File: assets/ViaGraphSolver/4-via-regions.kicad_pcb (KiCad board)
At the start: 2 copper layers, 0 parts

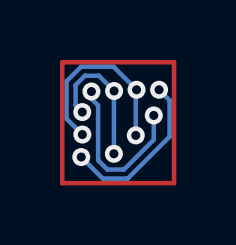
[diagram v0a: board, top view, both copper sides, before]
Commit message: Optimized 4  Via regions  Topology for  Improved Solve Performance
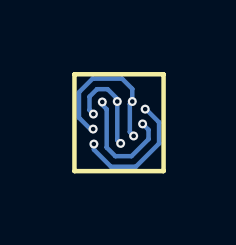
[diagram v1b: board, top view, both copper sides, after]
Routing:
- net net1: track 5.59 -> 3.92 mm
- net net4: track 4.71 -> 3.33 mm
- net net3: track 5.53 -> 4.27 mm
- net net5: track 6.40 -> 5.24 mm
